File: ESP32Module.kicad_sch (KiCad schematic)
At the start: 20 parts, among them IC4 ESP32-S3-MINI-1-N8, J8 USB_C_Receptacle, SW1 SW_SPST, SW2 SW_SPST

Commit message: fixing i2c pins to not be on strapping pins
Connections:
- net IO41 is gone; now on net SDA: IC4.37 (IO41)
- net IO42 is gone; now on net SCL: IC4.38 (IO42)
- net SCL: no longer IC4.44 (IO46)
- net SDA: no longer IC4.41 (IO45)
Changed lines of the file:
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@@
-    (effects (font (size 1.27 1.27)) (justify right))
-  )
-  (hierarchical_label "IO41" (shape input) (at 131.953 114.173 180)
     (effects (font (size 1.27 1.27)) (justify right))
   )
@@
     (effects (font (size 1.27 1.27)) (justify right))
   )
-  (hierarchical_label "SDA" (shape input) (at 164.973 30.353 0)
+  (hierarchical_label "SCL" (shape input) (at 164.973 22.733 0)
     (effects (font (size 1.27 1.27)) (justify left))
   )
@@
   (hierarchical_label "IO48" (shape input) (at 131.953 96.393 180)
     (effects (font (size 1.27 1.27)) (justify right))
-  )
-  (hierarchical_label "IO42" (shape input) (at 164.973 22.733 0)
-    (effects (font (size 1.27 1.27)) (justify left))
   )
   (hierarchical_label "SDA" (shape input) (at 189.23 129.54 90)
@@
     (effects (font (size 1.27 1.27)) (justify right))
   )
-  (hierarchical_label "SCL" (shape input) (at 164.973 37.973 0)
-    (effects (font (size 1.27 1.27)) (justify left))
+  (hierarchical_label "SDA" (shape input) (at 131.953 114.173 180)
+    (effects (font (size 1.27 1.27)) (justify right))
   )
   (hierarchical_label "IO11" (shape input) (at 131.953 58.293 180)

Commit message: Addressing the issues with the sample version, Updating the bom to source all the correct components from the JLCPCB supply
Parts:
- added C1: 0.1uF, Capacitor_SMD:C_0402_1005Metric, symbol Device:C
- TP14, TP15, TP5, TP6, TP7: now left out of the parts list
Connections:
- net GND: now also C1.2
- net IO0: now also C1.1
- net IO45: now reaches IC4.41 (IO45)
- net IO46: now reaches IC4.44 (IO46)
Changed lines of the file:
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@@
 (kicad_sch (version 20211123) (generator eeschema)
   (paper "A4")
+  (junction (at 217.17 128.27) (diameter 0) (color 0 0 0 0)
+  )
   (junction (at 164.973 60.833) (diameter 0) (color 0 0 0 0)
   )
@@
     (stroke (width 0) (type default) (color 0 0 0 0))
   )
+  (wire (pts (xy 227.33 125.73) (xy 227.33 129.794))
+    (stroke (width 0) (type default) (color 0 0 0 0))
+  )
   (wire (pts (xy 109.347 17.78) (xy 115.697 17.78))
     (stroke (width 0) (type default) (color 0 0 0 0))
@@
     (stroke (width 0) (type default) (color 0 0 0 0))
   )
+  (wire (pts (xy 218.313 129.794) (xy 217.17 129.794))
+    (stroke (width 0) (type default) (color 0 0 0 0))
+  )
   (wire (pts (xy 217.17 146.05) (xy 217.17 148.59))
     (stroke (width 0) (type default) (color 0 0 0 0))
@@
     (stroke (width 0) (type default) (color 0 0 0 0))
   )
+  (wire (pts (xy 225.933 129.794) (xy 227.33 129.794))
+    (stroke (width 0) (type default) (color 0 0 0 0))
+  )
   (wire (pts (xy 164.973 109.093) (xy 164.973 111.633))
     (stroke (width 0) (type default) (color 0 0 0 0))
@@
   )
   (wire (pts (xy 164.973 34.036) (xy 164.973 35.433))
+    (stroke (width 0) (type default) (color 0 0 0 0))
+  )
+  (wire (pts (xy 217.17 129.794) (xy 217.17 128.27))
     (stroke (width 0) (type default) (color 0 0 0 0))
   )
@@
     (effects (font (size 1.27 1.27)) (justify left))
   )
+  (hierarchical_label "IO46" (shape input) (at 164.973 37.973 0)
+    (effects (font (size 1.27 1.27)) (justify left))
+  )
   (hierarchical_label "IO2" (shape input) (at 131.953 35.433 180)
     (effects (font (size 1.27 1.27)) (justify right))
   )
+  (hierarchical_label "IO45" (shape input) (at 164.973 30.353 0)
+    (effects (font (size 1.27 1.27)) (justify left))
+  )
   (hierarchical_label "IO15" (shape input) (at 131.953 68.453 180)
     (effects (font (size 1.27 1.27)) (justify right))
@@
   )
   (symbol (lib_id "Connector:TestPoint") (at 226.06 24.13 0) (unit 1)
-    (in_bom yes) (on_board yes)
+    (in_bom no) (on_board yes)
     (property "Reference" "TP5" (id 0) (at 227.5332 21.1328 0)
       (effects (font (size 1.27 1.27)) (justify left))
@@
   )
   (symbol (lib_id "Connector:TestPoint") (at 226.06 35.56 0) (unit 1)
-    (in_bom yes) (on_board yes)
+    (in_bom no) (on_board yes)
     (property "Reference" "TP6" (id 0) (at 227.5332 32.5628 0)
       (effects (font (size 1.27 1.27)) (justify left))
@@
   )
   (symbol (lib_id "Connector:TestPoint") (at 240.03 35.56 0) (unit 1)
-    (in_bom yes) (on_board yes)
+    (in_bom no) (on_board yes)
     (property "Reference" "TP14" (id 0) (at 241.5032 32.5628 0)
       (effects (font (size 1.27 1.27)) (justify left))
@@
   )
   (symbol (lib_id "Connector:TestPoint") (at 254 35.56 0) (unit 1)
-    (in_bom yes) (on_board yes)
+    (in_bom no) (on_board yes)
     (property "Reference" "TP15" (id 0) (at 255.4732 32.5628 0)
       (effects (font (size 1.27 1.27)) (justify left))
@@
     (pin "9")
   )
+  (symbol (lib_id "Device:C") (at 222.123 129.794 270) (unit 1)
+    (in_bom yes) (on_board yes)
+    (property "Reference" "C1" (id 0) (at 218.313 132.334 90))
+    (property "Value" "0.1uF" (id 1) (at 224.663 132.334 90))
+    (property "Footprint" "Capacitor_SMD:C_0402_1005Metric" (id 2) (at 218.313 130.7592 0)
+      (effects (font (size 1.27 1.27)) hide)
+    )
+    (property "Datasheet" "~" (id 3) (at 222.123 129.794 0)
+      (effects (font (size 1.27 1.27)) hide)
+    )
+    (pin "1")
+    (pin "2")
+  )
   (symbol (lib_id "power:GND") (at 164.973 43.053 90) (unit 1)
     (in_bom yes) (on_board yes) (fields_autoplaced)
@@
   )
   (symbol (lib_id "Connector:TestPoint") (at 253.873 46.1518 0) (unit 1)
-    (in_bom yes) (on_board yes)
+    (in_bom no) (on_board yes)
     (property "Reference" "TP7" (id 0) (at 255.3462 43.1546 0)
       (effects (font (size 1.27 1.27)) (justify left))

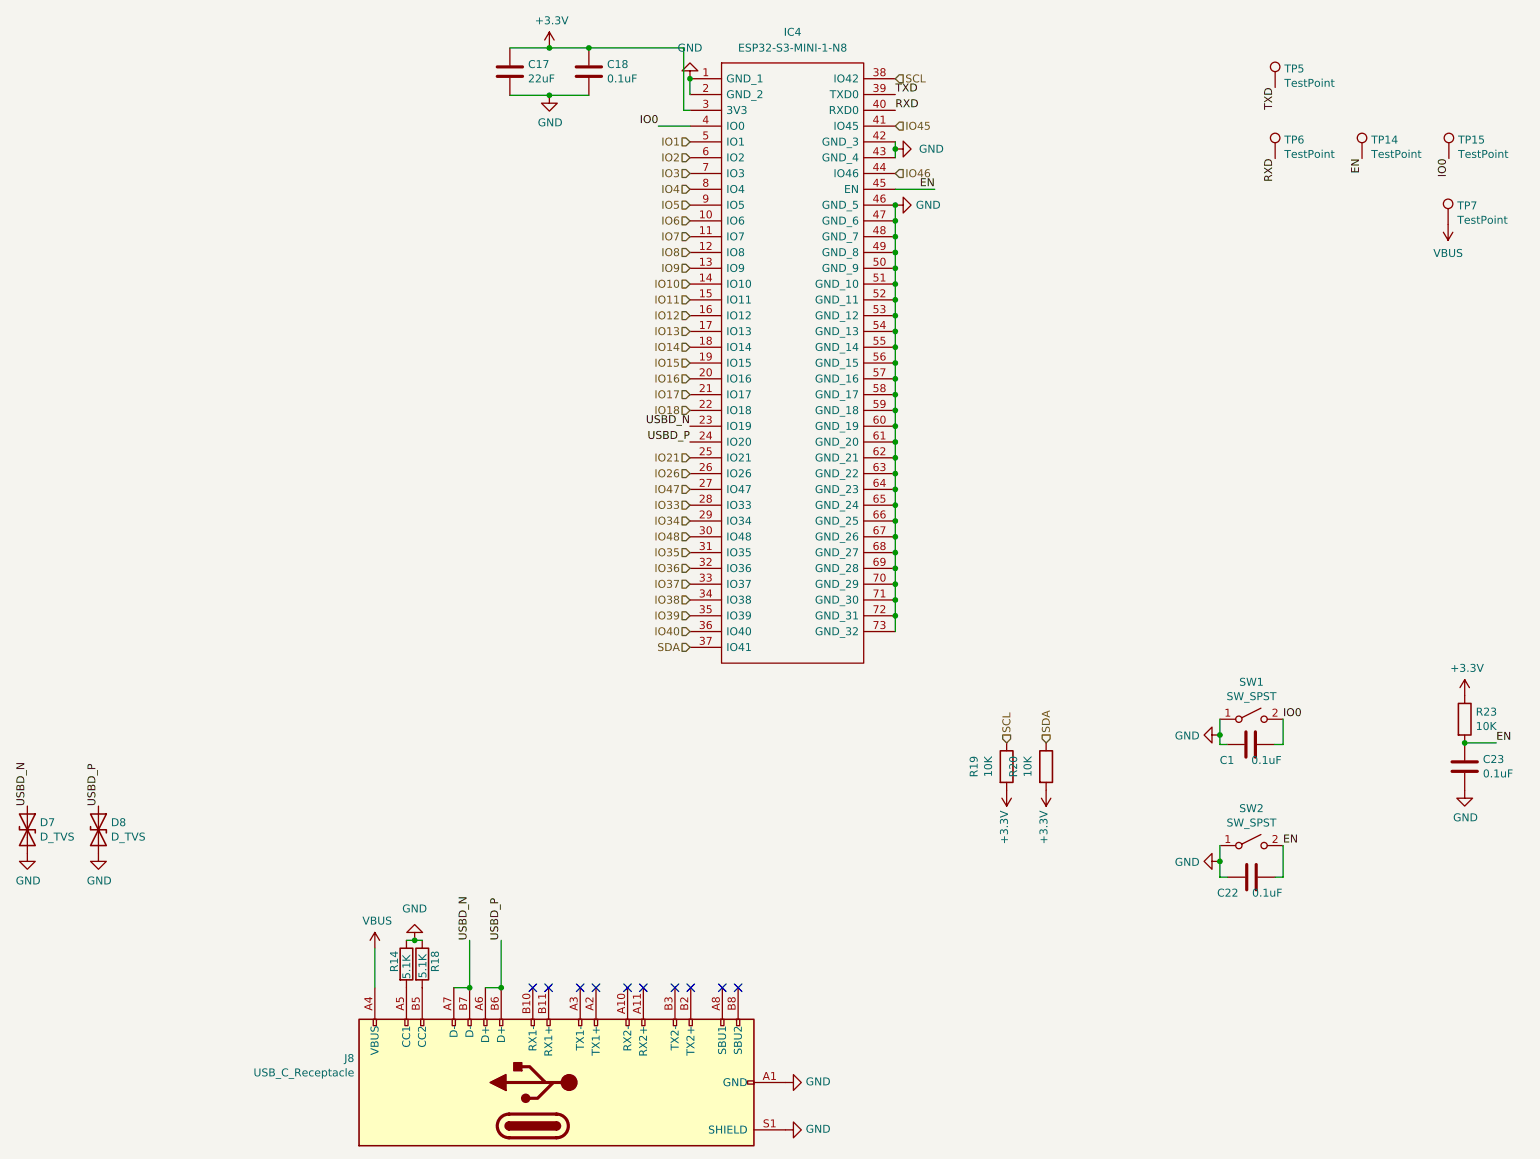
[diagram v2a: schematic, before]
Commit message: Adding usb c pd negotiation for battery charging
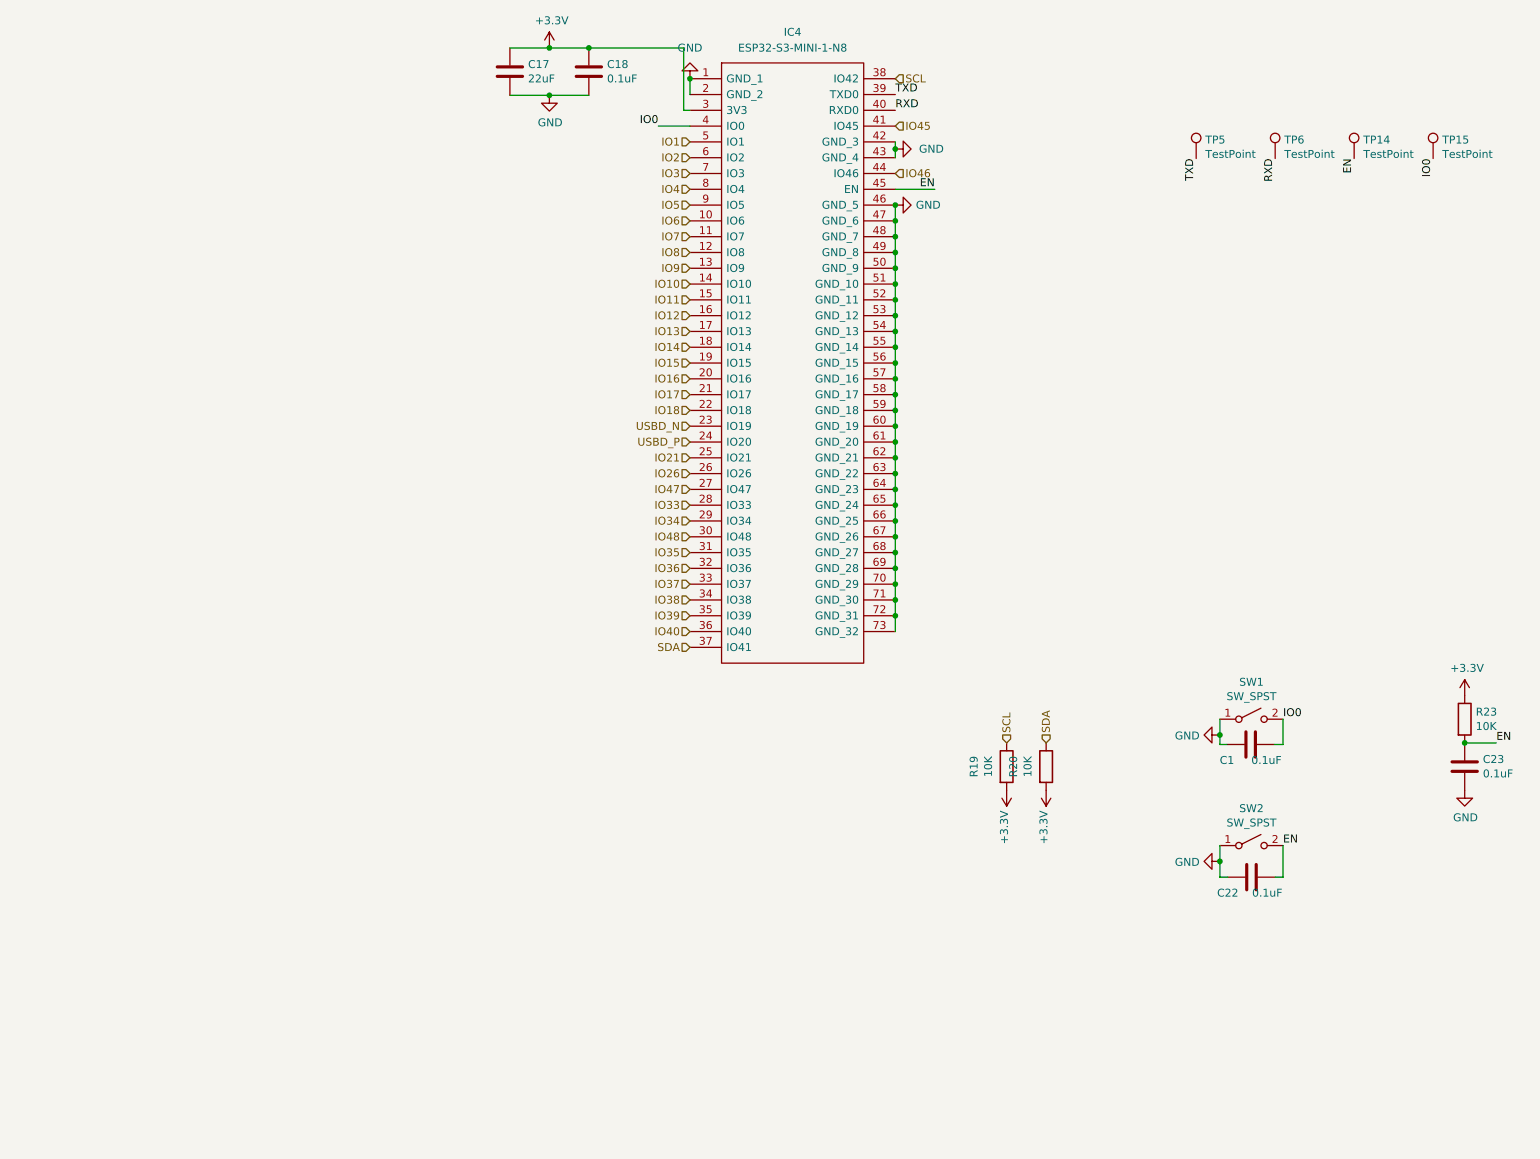
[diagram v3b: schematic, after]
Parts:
- removed D7, D8: D_TVS, Diode_SMD:D_SOD-523, symbol Device:D_TVS
- removed J8: USB_C_Receptacle, C167321:C167321, symbol SmallKat-v2-rescue:USB_C_Receptacle-Connector-SmallKat-v2-rescue-SmallKat-v2-re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
- removed R14, R18: 5.1K, Resistor_SMD:R_0402_1005Metric, symbol Device:R
- removed TP7: TestPoint, TestPoint:TestPoint_Pad_D2.0mm, symbol Connector:TestPoint
- IC4: footprint ESP32-s3-wroom-mini:ESP32S3MINI1N8 -> ESP32-S3-MINI:ESP32S3MINI1N8
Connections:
- no-connect marks 10 -> 0
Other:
- moved on the sheet: TP14, TP15, TP5
